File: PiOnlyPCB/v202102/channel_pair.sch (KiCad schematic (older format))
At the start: 7 parts, among them Q1 Q_NMOS_GDS, Q2 Q_NMOS_GDS, Q3 Dual_NMOSFET_BUK9K22_80E_Swap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

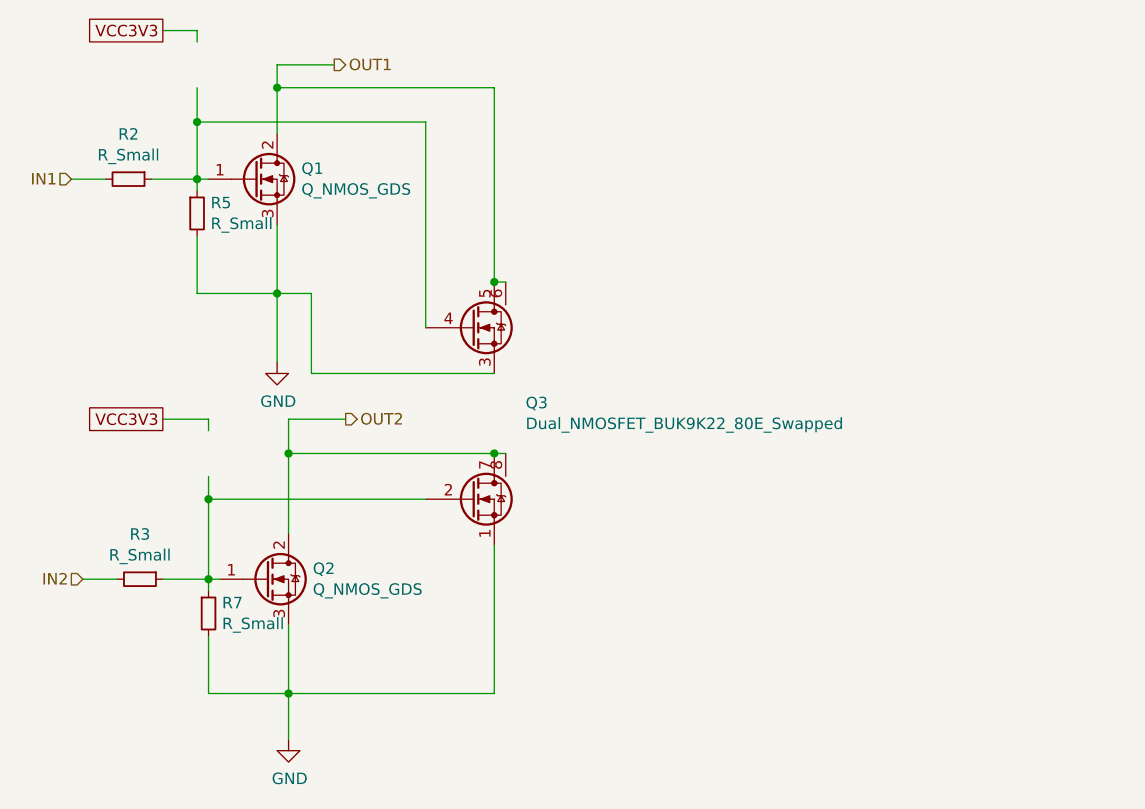
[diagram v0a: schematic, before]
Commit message: PiOnlyPCB 202102: Routed again without I2C expanders, before IN* nets routed.
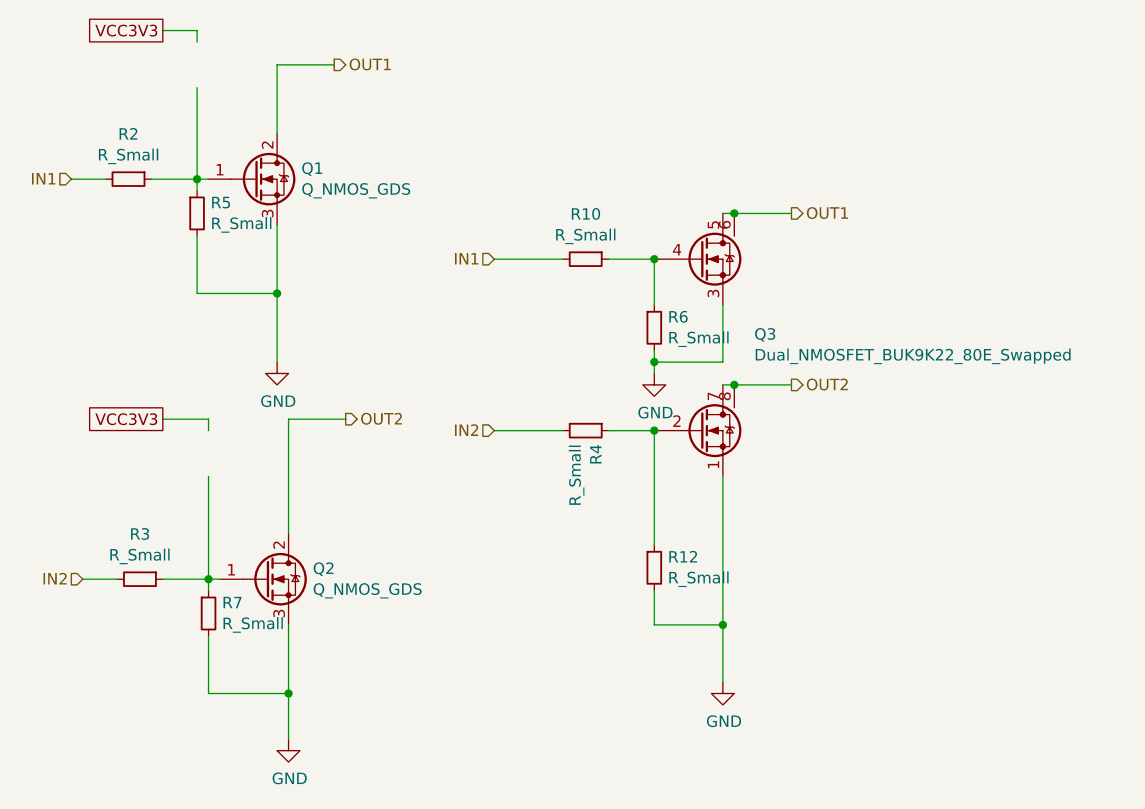
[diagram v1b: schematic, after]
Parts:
- added R10, R12, R4, R6: R_Small, Resistor_SMD:R_0805_2012Metric_Pad1.20x1.40mm_HandSolder, symbol Device:R_Small
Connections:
- wire segments 43 -> 44
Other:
- moved on the sheet: Q3

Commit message: PCB Ready to order. Passed DRC.
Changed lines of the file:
@@
 $Descr A4 11693 8268
 encoding utf-8
-Sheet 2 8
+Sheet 6 8
 Title ""
 Date ""
@@
 AR Path="/6024A3AD/60226CD2" Ref="R29"  Part="1"
 AR Path="/6024A6C1/60226CD2" Ref="R35"  Part="1"
-F 0 "R5" H 3159 2546 50  0000 L CNN
+F 0 "R29" H 3159 2546 50  0000 L CNN
 F 1 "R_Small" H 3159 2455 50  0000 L CNN
 F 2 "Resistor_SMD:R_0805_2012Metric_Pad1.20x1.40mm_HandSolder" H 3100 2500 50  0001 C CNN
@@
 AR Path="/6024A3AD/60226CD9" Ref="R26"  Part="1"
 AR Path="/6024A6C1/60226CD9" Ref="R32"  Part="1"
-F 0 "R2" V 2604 2350 50  0000 C CNN
+F 0 "R26" V 2604 2350 50  0000 C CNN
 F 1 "R_Small" V 2695 2350 50  0000 C CNN
 F 2 "Resistor_SMD:R_0805_2012Metric_Pad1.20x1.40mm_HandSolder" H 2800 2350 50  0001 C CNN
@@
 AR Path="/6024A3AD/60226CE8" Ref="#PWR011"  Part="1"
 AR Path="/6024A6C1/60226CE8" Ref="#PWR013"  Part="1"
-F 0 "#PWR03" H 3450 2900 50  0001 C CNN
+F 0 "#PWR011" H 3450 2900 50  0001 C CNN
 F 1 "GND" H 3455 2977 50  0000 C CNN
 F 2 "" H 3450 3150 50  0001 C CNN
@@
 AR Path="/6024A3AD/60226CFF" Ref="Q14"  Part="1"
 AR Path="/6024A6C1/60226CFF" Ref="Q17"  Part="1"
-F 0 "Q2" H 3606 4146 50  0000 L CNN
+F 0 "Q14" H 3606 4146 50  0000 L CNN
 F 1 "Q_NMOS_GDS" H 3606 4055 50  0000 L CNN
 F 2 "Package_TO_SOT_SMD:TO-252-2" H 3600 4200 50  0001 C CNN
@@
 AR Path="/6024A3AD/60226D0D" Ref="R31"  Part="1"
 AR Path="/6024A6C1/60226D0D" Ref="R37"  Part="1"
-F 0 "R7" H 3209 4296 50  0000 L CNN
+F 0 "R31" H 3209 4296 50  0000 L CNN
 F 1 "R_Small" H 3209 4205 50  0000 L CNN
 F 2 "Resistor_SMD:R_0805_2012Metric_Pad1.20x1.40mm_HandSolder" H 3150 4250 50  0001 C CNN
@@
 AR Path="/6024A3AD/60226D14" Ref="R27"  Part="1"
 AR Path="/6024A6C1/60226D14" Ref="R33"  Part="1"
-F 0 "R3" V 2654 4100 50  0000 C CNN
+F 0 "R27" V 2654 4100 50  0000 C CNN
 F 1 "R_Small" V 2745 4100 50  0000 C CNN
 F 2 "Resistor_SMD:R_0805_2012Metric_Pad1.20x1.40mm_HandSolder" H 2850 4100 50  0001 C CNN
@@
 AR Path="/6024A3AD/60226D23" Ref="#PWR012"  Part="1"
 AR Path="/6024A6C1/60226D23" Ref="#PWR014"  Part="1"
-F 0 "#PWR04" H 3500 4550 50  0001 C CNN
+F 0 "#PWR012" H 3500 4550 50  0001 C CNN
 F 1 "GND" H 3505 4627 50  0000 C CNN
 F 2 "" H 3500 4800 50  0001 C CNN
@@
 AR Path="/6024A3AD/603AAA71" Ref="R44"  Part="1"
 AR Path="/6024A6C1/603AAA71" Ref="R48"  Part="1"
-F 0 "R10" V 4604 2700 50  0000 C CNN
+F 0 "R44" V 4604 2700 50  0000 C CNN
 F 1 "R_Small" V 4695 2700 50  0000 C CNN
 F 2 "Resistor_SMD:R_0805_2012Metric_Pad1.20x1.40mm_HandSolder" H 4800 2700 50  0001 C CNN
@@
 AR Path="/6024A3AD/603B8C97" Ref="R45"  Part="1"
 AR Path="/6024A6C1/603B8C97" Ref="R49"  Part="1"
-F 0 "R12" H 5159 4096 50  0000 L CNN
+F 0 "R45" H 5159 4096 50  0000 L CNN
 F 1 "R_Small" H 5159 4005 50  0000 L CNN
 F 2 "Resistor_SMD:R_0805_2012Metric_Pad1.20x1.40mm_HandSolder" H 5100 4050 50  0001 C CNN
@@
 AR Path="/6024A3AD/603BA627" Ref="R42"  Part="1"
 AR Path="/6024A6C1/603BA627" Ref="R46"  Part="1"
-F 0 "R4" H 4859 3496 50  0000 L CNN
+F 0 "R42" H 4859 3496 50  0000 L CNN
 F 1 "R_Small" H 4859 3405 50  0000 L CNN
 F 2 "Resistor_SMD:R_0805_2012Metric_Pad1.20x1.40mm_HandSolder" H 4800 3450 50  0001 C CNN
@@
 AR Path="/6024A3AD/603BC177" Ref="R43"  Part="1"
 AR Path="/6024A6C1/603BC177" Ref="R47"  Part="1"
-F 0 "R6" H 5159 3046 50  0000 L CNN
+F 0 "R43" H 5159 3046 50  0000 L CNN
 F 1 "R_Small" H 5159 2955 50  0000 L CNN
 F 2 "Resistor_SMD:R_0805_2012Metric_Pad1.20x1.40mm_HandSolder" H 5100 3000 50  0001 C CNN
@@
 AR Path="/6024A3AD/60226CC4" Ref="Q13"  Part="1"
 AR Path="/6024A6C1/60226CC4" Ref="Q16"  Part="1"
-F 0 "Q1" H 3556 2396 50  0000 L CNN
+F 0 "Q13" H 3556 2396 50  0000 L CNN
 F 1 "Q_NMOS_GDS" H 3556 2305 50  0000 L CNN
 F 2 "Package_TO_SOT_SMD:TO-252-2" H 3550 2450 50  0001 C CNN
@@
 P 5400 4550
 AR Path="/603E2FDA" Ref="#PWR?"  Part="1"
-AR Path="/602264F6/603E2FDA" Ref="#PWR?"  Part="1"
-AR Path="/60215F23/603E2FDA" Ref="#PWR?"  Part="1"
-AR Path="/60228E98/603E2FDA" Ref="#PWR?"  Part="1"
-AR Path="/602291AC/603E2FDA" Ref="#PWR?"  Part="1"
-AR Path="/6024A3AD/603E2FDA" Ref="#PWR?"  Part="1"
-AR Path="/6024A6C1/603E2FDA" Ref="#PWR?"  Part="1"
-F 0 "#PWR?" H 5400 4300 50  0001 C CNN
+AR Path="/602264F6/603E2FDA" Ref="#PWR0101"  Part="1"
+AR Path="/60215F23/603E2FDA" Ref="#PWR0103"  Part="1"
+AR Path="/60228E98/603E2FDA" Ref="#PWR0105"  Part="1"
+AR Path="/602291AC/603E2FDA" Ref="#PWR0107"  Part="1"
+AR Path="/6024A3AD/603E2FDA" Ref="#PWR0109"  Part="1"
+AR Path="/6024A6C1/603E2FDA" Ref="#PWR0111"  Part="1"
+F 0 "#PWR0109" H 5400 4300 50  0001 C CNN
 F 1 "GND" H 5405 4377 50  0000 C CNN
 F 2 "" H 5400 4550 50  0001 C CNN
@@
 P 5100 3200
 AR Path="/603E374E" Ref="#PWR?"  Part="1"
-AR Path="/602264F6/603E374E" Ref="#PWR?"  Part="1"
-AR Path="/60215F23/603E374E" Ref="#PWR?"  Part="1"
-AR Path="/60228E98/603E374E" Ref="#PWR?"  Part="1"
-AR Path="/602291AC/603E374E" Ref="#PWR?"  Part="1"
-AR Path="/6024A3AD/603E374E" Ref="#PWR?"  Part="1"
-AR Path="/6024A6C1/603E374E" Ref="#PWR?"  Part="1"
-F 0 "#PWR?" H 5100 2950 50  0001 C CNN
+AR Path="/602264F6/603E374E" Ref="#PWR0102"  Part="1"
+AR Path="/60215F23/603E374E" Ref="#PWR0104"  Part="1"
+AR Path="/60228E98/603E374E" Ref="#PWR0106"  Part="1"
+AR Path="/602291AC/603E374E" Ref="#PWR0108"  Part="1"
+AR Path="/6024A3AD/603E374E" Ref="#PWR0110"  Part="1"
+AR Path="/6024A6C1/603E374E" Ref="#PWR0112"  Part="1"
+F 0 "#PWR0110" H 5100 2950 50  0001 C CNN
 F 1 "GND" H 5105 3027 50  0000 C CNN
 F 2 "" H 5100 3200 50  0001 C CNN
@@
 AR Path="/6024A3AD/60228931" Ref="Q15"  Part="1"
 AR Path="/6024A6C1/60228931" Ref="Q18"  Part="1"
-F 0 "Q3" H 5537 3171 50  0000 L CNN
+F 0 "Q15" H 5537 3171 50  0000 L CNN
 F 1 "Dual_NMOSFET_BUK9K22_80E_Swapped" H 5537 3080 50  0000 L CNN
 F 2 "v202102_OpenPlant:LFPAK56D" H 5500 3600 50  0001 C CNN
